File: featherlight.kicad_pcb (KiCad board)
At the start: 4 copper layers, 50.8 x 50.8 mm, 106 parts, among them P1 USB_OTG, P11 CONN_01X06, P12 CONN_01X06, P13 CONN_01X06, P14 CONN_01X06, P15 CONN_01X06, P16 CONN_01X06, P17 CONN_01X06, P2 CONN_01X02, P3 CONN_01X01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

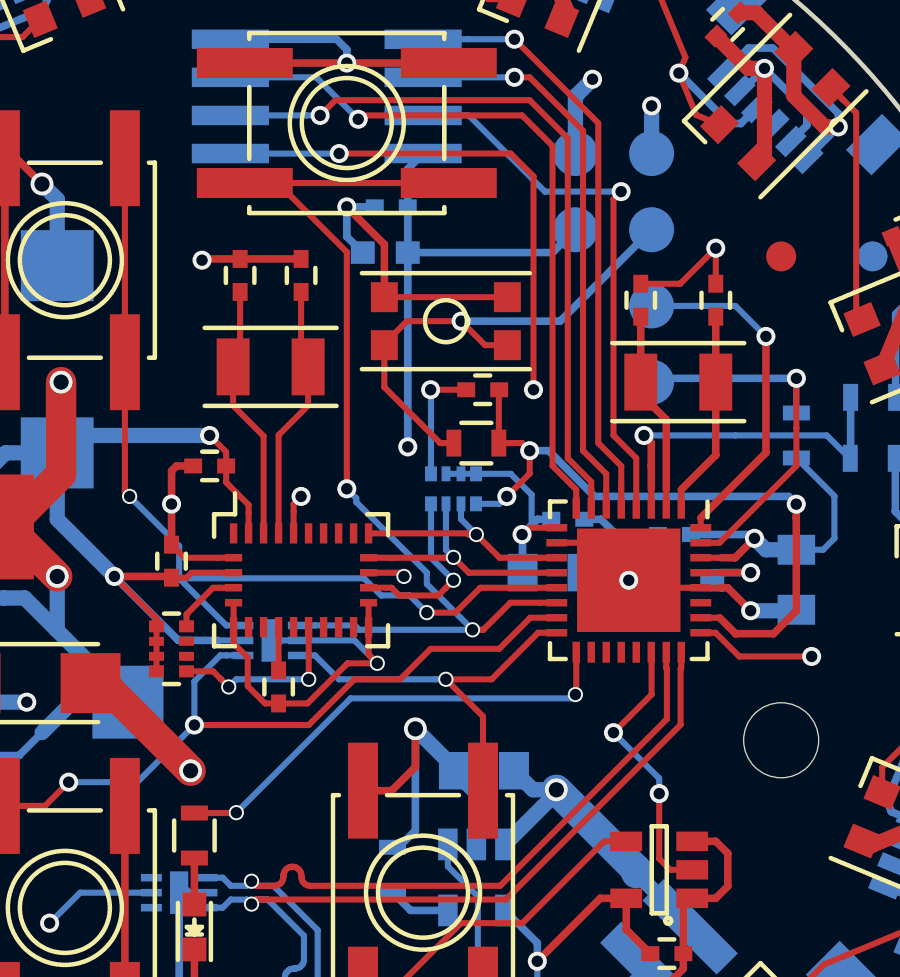
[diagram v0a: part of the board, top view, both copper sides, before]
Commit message: Put MCU analog ground and VDD on dedicated vias after reading a bit about analog PCB design.
http://www.edn.com/design/pc-board/4443239/Properly-ground-your-circuits
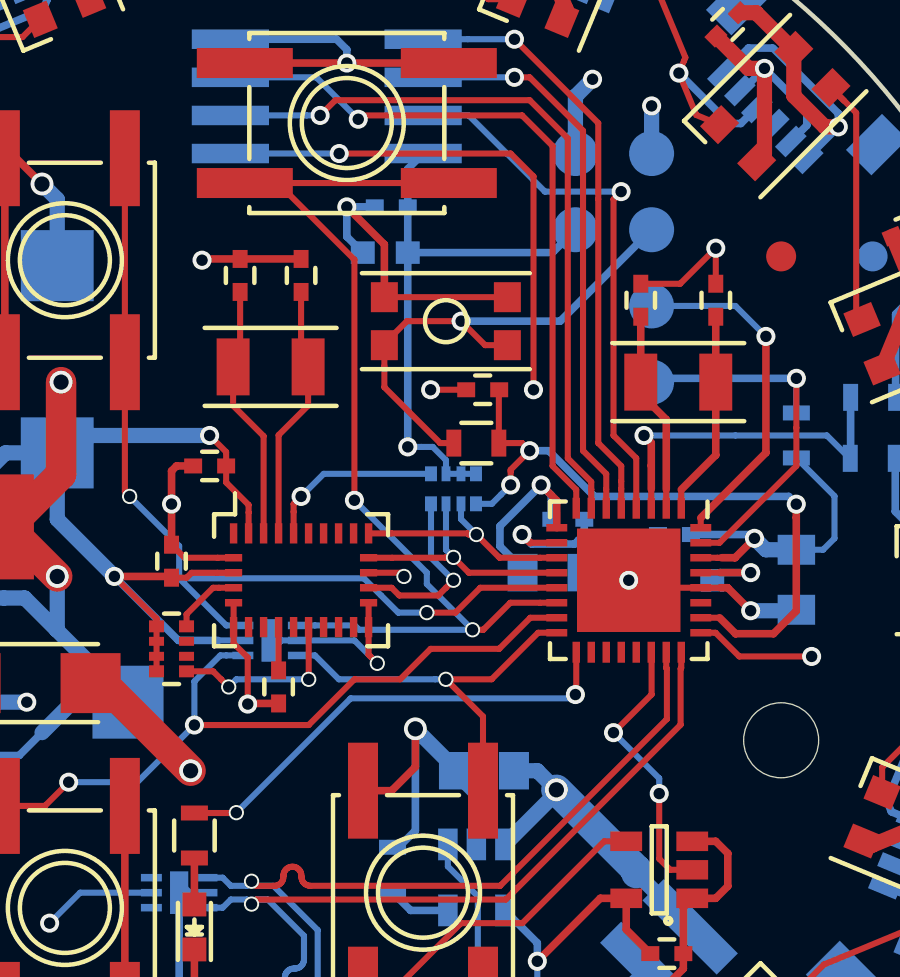
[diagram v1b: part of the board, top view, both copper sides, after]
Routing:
- net GND: track 300.4 -> 298.5 mm, vias 34 -> 36
- net +3V3: track 66.7 -> 67.9 mm

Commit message: Rev E
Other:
- board text added: "Featherlight Rev E"
- board text removed: "Featherlight Rev D"
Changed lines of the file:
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@@
     (arrow2b (pts (xy 117.602 130.048) (xy 116.475496 130.634421)))
   )
-  (gr_text "Featherlight\nRev D" (at 92.075 114.935) (layer B.SilkS)
+  (gr_text "Featherlight\nRev E" (at 92.075 114.935) (layer B.SilkS)
     (effects (font (size 1 1) (thickness 0.15)) (justify mirror))
   )

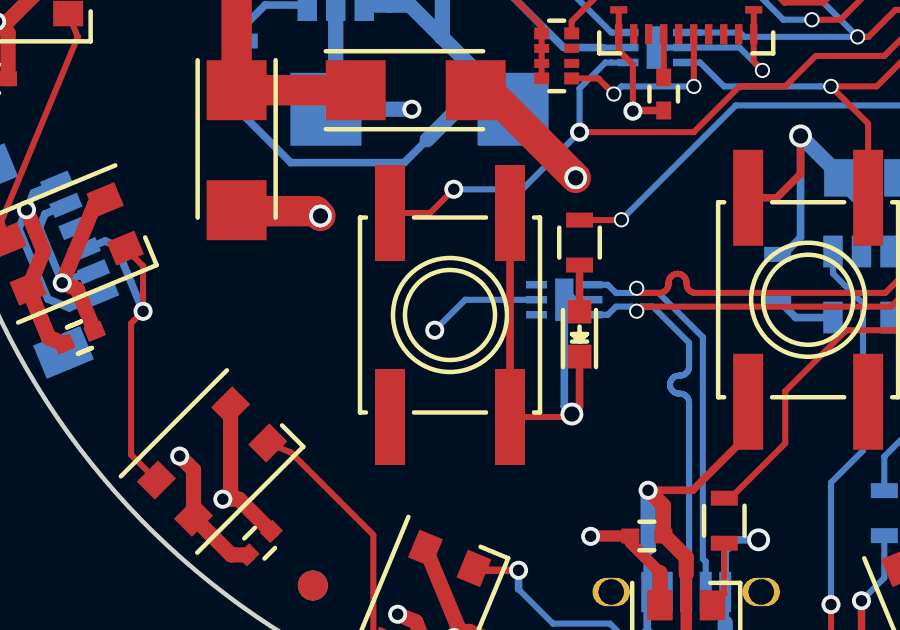
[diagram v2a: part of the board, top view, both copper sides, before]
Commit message: Moved via to the side of the internal power trace.
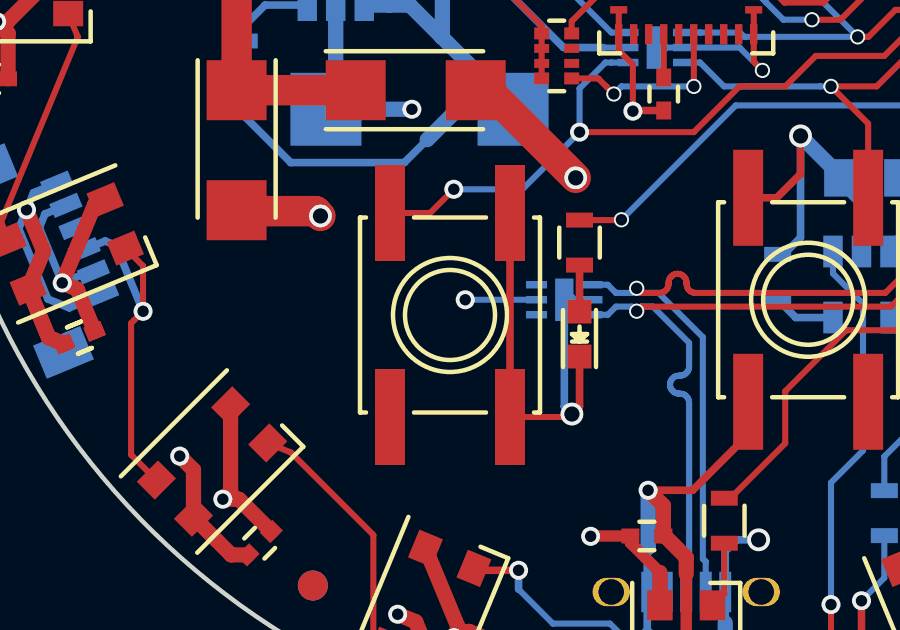
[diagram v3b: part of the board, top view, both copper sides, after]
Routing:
- net /Power Regulation & Distribution/VUSB: track 36.0 -> 44.4 mm
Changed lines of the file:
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@@
-(kicad_pcb (version 20160815) (host pcbnew no-vcs-found-7500~57~ubuntu16.10.1)
+(kicad_pcb (version 20160815) (host pcbnew no-vcs-found-7520~57~ubuntu16.10.1)
   (general
     (links 278)
@@
     (thickness 1.6002)
     (drawings 92)
-    (tracks 1082)
+    (tracks 1091)
     (zones 0)
     (modules 106)
@@
   (segment (start 106.492 110.406) (end 106.492 111.1392) (width 0.2032) (layer B.Cu) (net 52) (status 10))
   (segment (start 106.492 111.1392) (end 107.49281 112.14001) (width 0.2032) (layer B.Cu) (net 52))
-  (via (at 93.218 113.03) (size 0.635) (drill 0.381) (layers F.Cu B.Cu) (net 53))
-  (segment (start 94.234 112.014) (end 93.218 113.03) (width 0.2032) (layer B.Cu) (net 53))
+  (segment (start 104.013 120.015) (end 101.726999 120.015) (width 1.016) (layer Split_Power) (net 53))
+  (segment (start 101.726999 120.015) (end 101.418134 119.706135) (width 1.016) (layer Split_Power) (net 53))
+  (segment (start 103.632001 119.634001) (end 101.346 119.634001) (width 1.016) (layer Split_Power) (net 53))
+  (segment (start 101.346 119.634001) (end 99.822001 119.634001) (width 1.016) (layer Split_Power) (net 53))
+  (segment (start 101.418134 121.230134) (end 101.418134 119.706135) (width 1.016) (layer Split_Power) (net 53))
+  (segment (start 101.418134 119.706135) (end 101.346 119.634001) (width 1.016) (layer Split_Power) (net 53))
+  (segment (start 89.408 109.22) (end 92.202 112.014) (width 1.016) (layer Split_Power) (net 53))
+  (segment (start 92.202 112.014) (end 93.218 113.03) (width 1.016) (layer Split_Power) (net 53))
+  (segment (start 94.234 112.014) (end 92.202 112.014) (width 1.016) (layer Split_Power) (net 53))
+  (segment (start 94.234 112.014) (end 93.218 113.03) (width 1.016) (layer Split_Power) (net 53))
+  (segment (start 94.234 114.046) (end 93.218 113.03) (width 1.016) (layer Split_Power) (net 53))
+  (segment (start 99.822 119.634) (end 94.234 114.046) (width 1.016) (layer Split_Power) (net 53))
+  (segment (start 94.234 114.046) (end 94.234 112.014) (width 1.016) (layer Split_Power) (net 53))
+  (via (at 94.234 112.014) (size 0.635) (drill 0.381) (layers F.Cu B.Cu) (net 53))
   (segment (start 93.218 113.03) (end 93.163134 113.03) (width 0.2032) (layer Split_Power) (net 53))
-  (segment (start 99.822 119.634) (end 93.218 113.03) (width 1.016) (layer Split_Power) (net 53))
-  (segment (start 89.408 109.22) (end 93.218 113.03) (width 1.016) (layer Split_Power) (net 53))
   (segment (start 96.611 112.014) (end 94.234 112.014) (width 0.2032) (layer B.Cu) (net 53) (status 10))
   (segment (start 102.9 121.75446) (end 102.9 120.396) (width 0.254) (layer B.Cu) (net 53))
@@
   (via (at 89.408 109.22) (size 0.762) (drill 0.508) (layers F.Cu B.Cu) (net 53))
   (segment (start 101.418134 121.230134) (end 99.822 119.634) (width 1.016) (layer Split_Power) (net 53))
-  (segment (start 103.632001 119.634001) (end 99.822001 119.634001) (width 1.016) (layer Split_Power) (net 53))
   (segment (start 99.822001 119.634001) (end 99.822 119.634) (width 1.016) (layer Split_Power) (net 53))
   (segment (start 90.583 105.029) (end 86.614 105.029) (width 1.016) (layer F.Cu) (net 54))

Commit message: Reduced global solder mask pullback to 0.05 mm to address solder briding issues on some of the components.
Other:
- rule pad_to_mask_clearance: 0.2 -> 0.05
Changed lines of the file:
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@@
     (pad_size 2 2)
     (pad_drill 0)
-    (pad_to_mask_clearance 0.2)
+    (pad_to_mask_clearance 0.05)
+    (solder_mask_min_width 0.127)
     (pad_to_paste_clearance_ratio -0.1835)
     (aux_axis_origin 57.15 57.15)
